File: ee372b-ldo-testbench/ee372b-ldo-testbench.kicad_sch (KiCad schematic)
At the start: 136 parts, among them J1 PEC02SAAN, J10 OUT_S, J11 VOUT, J12 VDD_BUF, J13 V_SIG, J14 PEC03SAAN, J15 VSIG_BUF, J16 PEC03SAAN, J17 PEC03SAAN, J18 PEC03SAAN, J19 PEC03SAAN, J2 PEC02SAAN, J20 VREF_EXTERNAL, J21 PEC02SAAN, J22 PEC02SAAN, J23 PEC02SAAN, J24 PEC02SAAN, J25 PEC03SAAN, J3 GND, J4 1V8, J5 3v3_EXTERNAL, J8 VIN, J9 IN_S, Q1 FDV305N, Q2 FDV305N, Q3 FDV305N, Q4 FDV305N, Q5 FDV305N, U1 MMSZ4679T1G, U3 ADS1220IPW, U4 BUF634AIDR

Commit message: reduced pin bypass caps
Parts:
- removed C24, C9: 100nF, Capacitor_SMD:C_0805_2012Metric_Pad1.18x1.45mm_HandSolder, symbol Device:C_Small_US
- removed R21, R22, R23, R24, R25, R26, R27, R28, R29, R30, R31, R32, R33, R34, R35, R36: 0, Resistor_SMD:R_0805_2012Metric_Pad1.20x1.40mm_HandSolder, symbol Device:R
- added R45, R46: 0, Resistor_SMD:R_0805_2012Metric_Pad1.20x1.40mm_HandSolder, symbol Device:R
- C27: value 1uF -> 100nF
- C6: value 100nF -> 1uF
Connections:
- net GND: now also U2.1 (VSS), U2.13 (VSS), U2.18 (VSS), U2.20 (VSS), U2.22 (VSS), U2.23 (VSS), U2.25 (VSS), U2.26 (VSS), U2.28 (VSS), U2.29 (VSS), U2.3 (VSS), U2.30 (VSS), U2.31 (VSS), U2.4 (VSS), U2.6 (VSS), U2.7 (VSS), R46.2; no longer U3.6 (AIN3/REFN1)
- net c1_vin_jump: now also R45.1; no longer C4.2, U2.2 (VDD)
- net at C23.2, U2.27 (VDD): now also C10.2, C17.2, C27.2, C4.2, C5.2, C6.2, C7.2, U2.14 (VDD), U2.16 (VDD), U2.17 (VDD), U2.2 (VDD), U2.21 (VDD), U2.24 (VDD), U2.32 (VDD), U2.8 (VDD), R45.2
- new net LDO_GND: R46.1, U3.6 (AIN3/REFN1)
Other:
- moved on the sheet: C10, C23, C27, C4, C5, C7

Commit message: added 100mm x 100mm thing
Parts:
- removed J8: VIN, 1_EE372_DemoBoard:CALTEST_CT3151-2, symbol Connector:Conn_01x01_Pin
- removed R57: 0, Resistor_SMD:R_0805_2012Metric_Pad1.20x1.40mm_HandSolder, symbol Device:R
- TP10: value 1V8 -> 3V3
- TP3: value OUT_S1 -> LOAD_OUT
- TP4: value OUT_S2 -> LDO_VOUT
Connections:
- net BGR_VREF: now also R37.2, U2.19 (OTA_VREF)
- net VIN renamed 1V8
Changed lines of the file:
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@@
 	(wire
 		(pts
-			(xy 334.01 115.57) (xy 336.55 115.57)
-		)
-		(stroke
-			(width 0)
-			(type default)
-		)
-	)
-	(wire
-		(pts
 			(xy 377.19 135.89) (xy 379.73 135.89)
 		)
@@
 	(wire
 		(pts
-			(xy 323.85 115.57) (xy 326.39 115.57)
+			(xy 323.85 115.57) (xy 336.55 115.57)
 		)
 		(stroke
@@
 		)
 	)
+	(label "1V8"
+		(at 172.72 80.01 0)
+		(effects
+			(font
+				(size 1.27 1.27)
+			)
+			(justify left bottom)
+		)
+	)
 	(label "pico_spi_tx"
 		(at 365.76 285.75 180)
@@
 			)
 		)
-		(property "Value" "OUT_S1"
+		(property "Value" "LOAD_OUT"
 			(at 523.24 105.9179 0)
 			(show_name no)
@@
 	)
 	(symbol
-		(lib_id "Device:R")
-		(at 330.2 115.57 270)
-		(unit 1)
-		(body_style 1)
-		(exclude_from_sim no)
-		(in_bom yes)
-		(on_board yes)
-		(in_pos_files yes)
-		(dnp no)
-		(fields_autoplaced yes)
-		(property "Reference" "R57"
-			(at 330.2 109.22 90)
-			(show_name no)
-			(do_not_autoplace no)
-			(effects
-				(font
-					(size 1.27 1.27)
-				)
-			)
-		)
-		(property "Value" "0"
-			(at 330.2 111.76 90)
-			(show_name no)
-			(do_not_autoplace no)
-			(effects
-				(font
-					(size 1.27 1.27)
-				)
-			)
-		)
-		(property "Footprint" "Resistor_SMD:R_0805_2012Metric_Pad1.20x1.40mm_HandSolder"
-			(at 330.2 113.792 90)
-			(hide yes)
-			(show_name no)
-			(do_not_autoplace no)
-			(effects
-				(font
-					(size 1.27 1.27)
-				)
-			)
-		)
-		(property "Datasheet" ""
-			(at 330.2 115.57 0)
-			(hide yes)
-			(show_name no)
-			(do_not_autoplace no)
-			(effects
-				(font
-					(size 1.27 1.27)
-				)
-			)
-		)
-		(property "Description" "Resistor"
-			(at 330.2 115.57 0)
-			(hide yes)
-			(show_name no)
-			(do_not_autoplace no)
-			(effects
-				(font
-					(size 1.27 1.27)
-				)
-			)
-		)
-		(pin "1"
-		)
-		(pin "2"
-		)
-		(instances
-			(project "ee372b-ldo-testbench"
-				(path "/4eaac8a8-2761-424f-b17c-d4cc8c253812"
-					(reference "R57")
-					(unit 1)
-				)
-			)
-		)
-	)
-	(symbol
 		(lib_id "power:GND")
 		(at 194.31 92.71 0)
@@
 			)
 		)
-		(property "Value" "OUT_S2"
+		(property "Value" "LDO_VOUT"
 			(at 492.76 104.6479 0)
 			(show_name no)
@@
 	)
 	(symbol
-		(lib_id "Connector:Conn_01x01_Pin")
-		(at 167.64 80.01 0)
-		(unit 1)
-		(body_style 1)
-		(exclude_from_sim no)
-		(in_bom yes)
-		(on_board yes)
-		(in_pos_files yes)
-		(dnp no)
-		(property "Reference" "J8"
-			(at 168.275 74.93 0)
-			(show_name no)
-			(do_not_autoplace no)
-			(effects
-				(font
-					(size 1.27 1.27)
-				)
-			)
-		)
-		(property "Value" "VIN"
-			(at 168.275 77.47 0)
-			(show_name no)
-			(do_not_autoplace no)
-			(effects
-				(font
-					(size 1.27 1.27)
-				)
-			)
-		)
-		(property "Footprint" "1_EE372_DemoBoard:CALTEST_CT3151-2"
-			(at 167.64 80.01 0)
-			(hide yes)
-			(show_name no)
-			(do_not_autoplace no)
-			(effects
-				(font
-					(size 1.27 1.27)
-				)
-			)
-		)
-		(property "Datasheet" "https://mm.digikey.com/Volume0/opasdata/d220001/medias/docus/4846/DS_1768_Catalog.pdf"
-			(at 167.64 80.01 0)
-			(hide yes)
-			(show_name no)
-			(do_not_autoplace no)
-			(effects
-				(font
-					(size 1.27 1.27)
-				)
-			)
-		)
-		(property "Description" "CONN BANANA JACK SOLDER RED"
-			(at 167.64 80.01 0)
-			(hide yes)
-			(show_name no)
-			(do_not_autoplace no)
-			(effects
-				(font
-					(size 1.27 1.27)
-				)
-			)
-		)
-		(property "Manufacturer" "Cal Test Electronics"
-			(at 167.64 80.01 0)
-			(hide yes)
-			(show_name no)
-			(do_not_autoplace no)
-			(effects
-				(font
-					(size 1.27 1.27)
-				)
-			)
-		)
-		(property "Manufacturer Part Number" "CT3151SP-2"
-			(at 167.64 80.01 0)
-			(hide yes)
-			(show_name no)
-			(do_not_autoplace no)
-			(effects
-				(font
-					(size 1.27 1.27)
-				)
-			)
-		)
-		(property "Distributer Link 1" "https://www.digikey.com/en/products/detail/cal-test-electronics/CT3151SP-2/6005547"
-			(at 167.64 80.01 0)
-			(hide yes)
-			(show_name no)
-			(do_not_autoplace no)
-			(effects
-				(font
-					(size 1.27 1.27)
-				)
-			)
-		)
-		(property "Distributer Link 2" "https://www.mouser.com/en/ProductDetail/Cal-Test/CT3151SP-2?qs=vgjKjNJexTiE58m2a2m1iA%3D%3D"
-			(at 167.64 80.01 0)
-			(hide yes)
-			(show_name no)
-			(do_not_autoplace no)
-			(effects
-				(font
-					(size 1.27 1.27)
-				)
-			)
-		)
-		(pin "1"
-		)
-		(instances
-			(project "ee372b-ldo-testbench"
-				(path "/4eaac8a8-2761-424f-b17c-d4cc8c253812"
-					(reference "J8")
-					(unit 1)
-				)
-			)
-		)
-	)
-	(symbol
 		(lib_id "power:GND")
 		(at 434.34 316.23 0)
@@
 			)
 		)
-		(property "Value" "1V8"
+		(property "Value" "3V3"
 			(at 265.43 198.6279 0)
 			(show_name no)

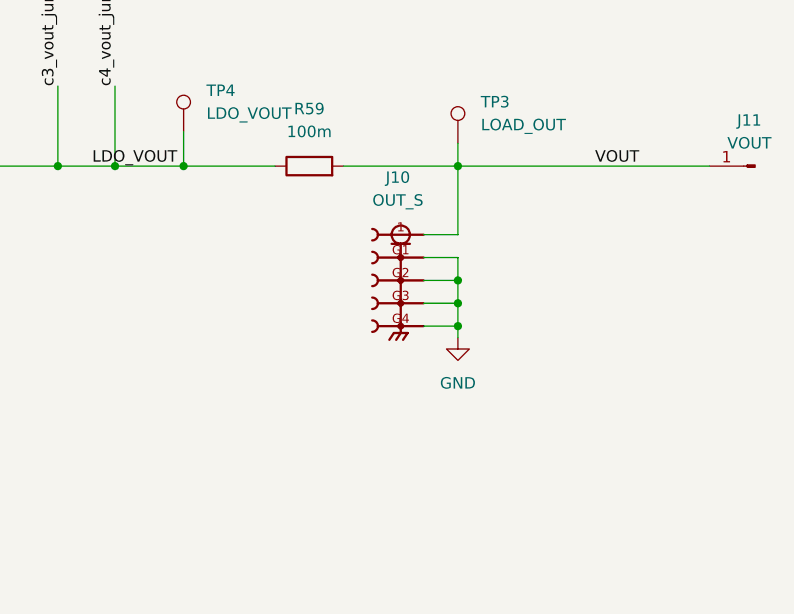
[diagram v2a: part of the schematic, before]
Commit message: added selectable output for ADC Analog3 pin measurement for VOUT
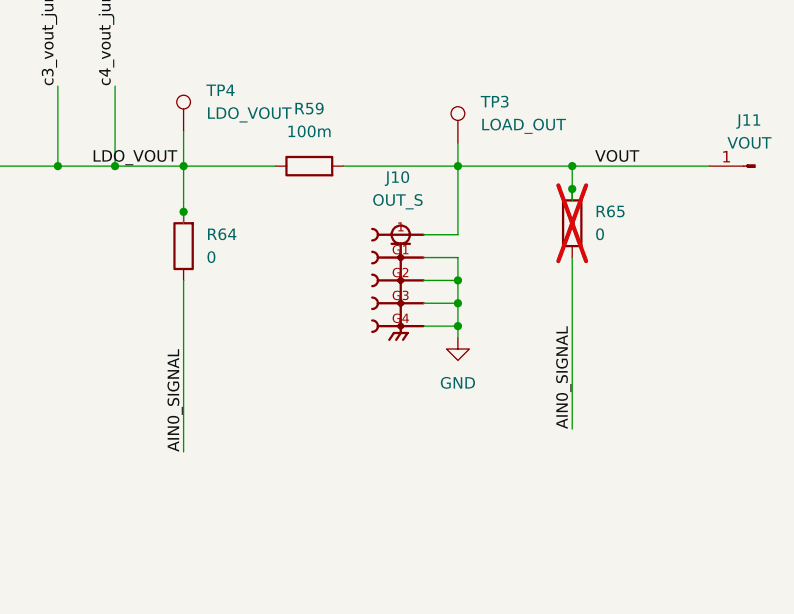
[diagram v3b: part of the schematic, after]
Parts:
- added R64, R65: 0, Resistor_SMD:R_0805_2012Metric_Pad1.20x1.40mm_HandSolder, symbol Device:R
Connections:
- net AIN0_SIGNAL: now also R64.1, R65.1
- net LDO_VOUT: now also R64.2
- net VOUT: now also R65.2

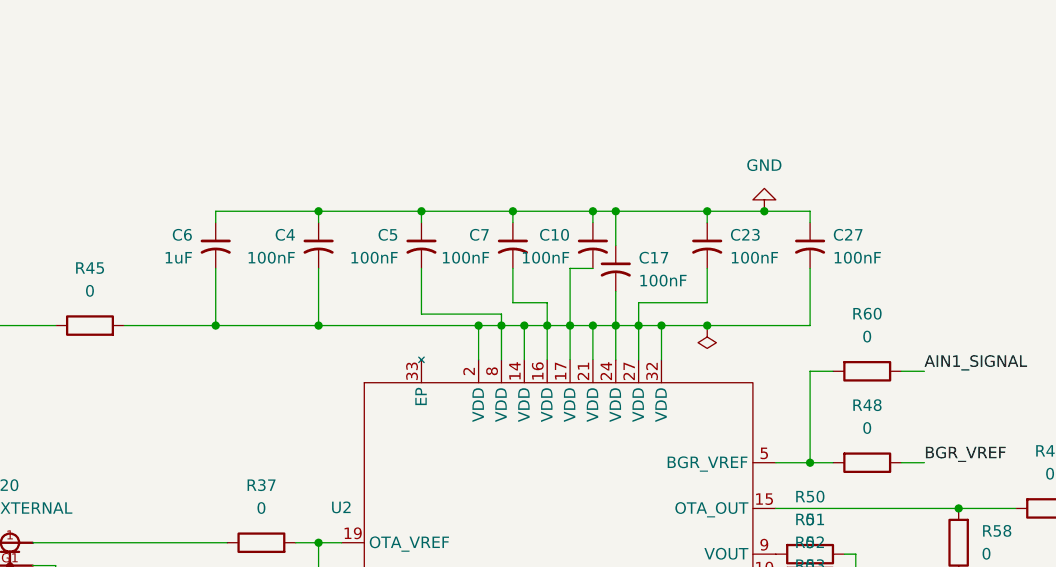
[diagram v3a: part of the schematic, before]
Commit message: re add caps for each pin
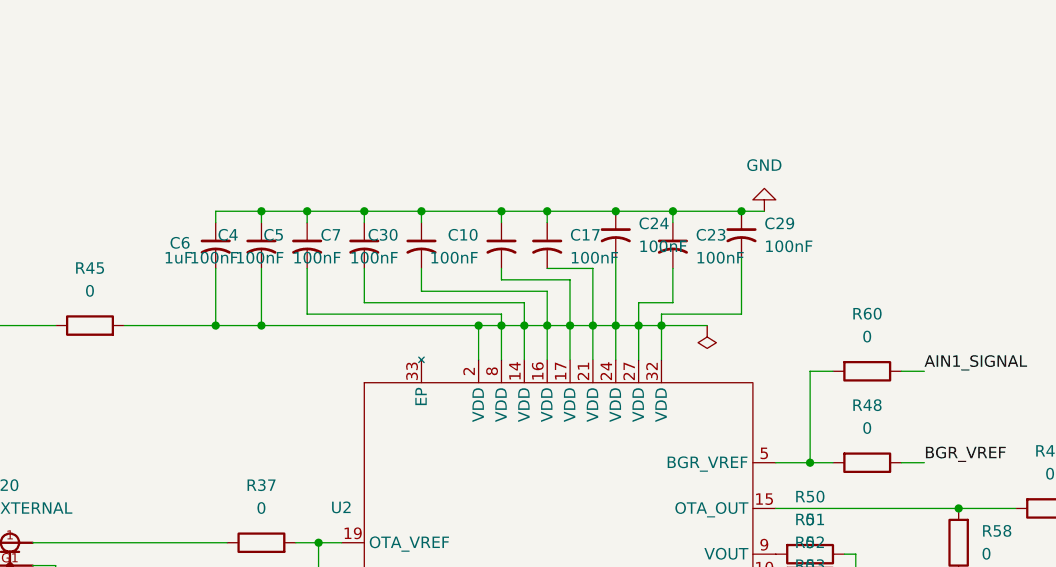
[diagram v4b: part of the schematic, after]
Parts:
- removed C27: 100nF, Capacitor_SMD:C_0805_2012Metric_Pad1.18x1.45mm_HandSolder, symbol Device:C_Small_US
- added C24, C29, C30: 100nF, Capacitor_SMD:C_0805_2012Metric_Pad1.18x1.45mm_HandSolder, symbol Device:C_Small_US
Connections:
- net GND: now also C24.1, C29.1, C30.1
- net at C10.2, C17.2, C23.2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: now also C24.2, C29.2, C30.2
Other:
- moved on the sheet: C10, C17, C23, C4, C5, C7

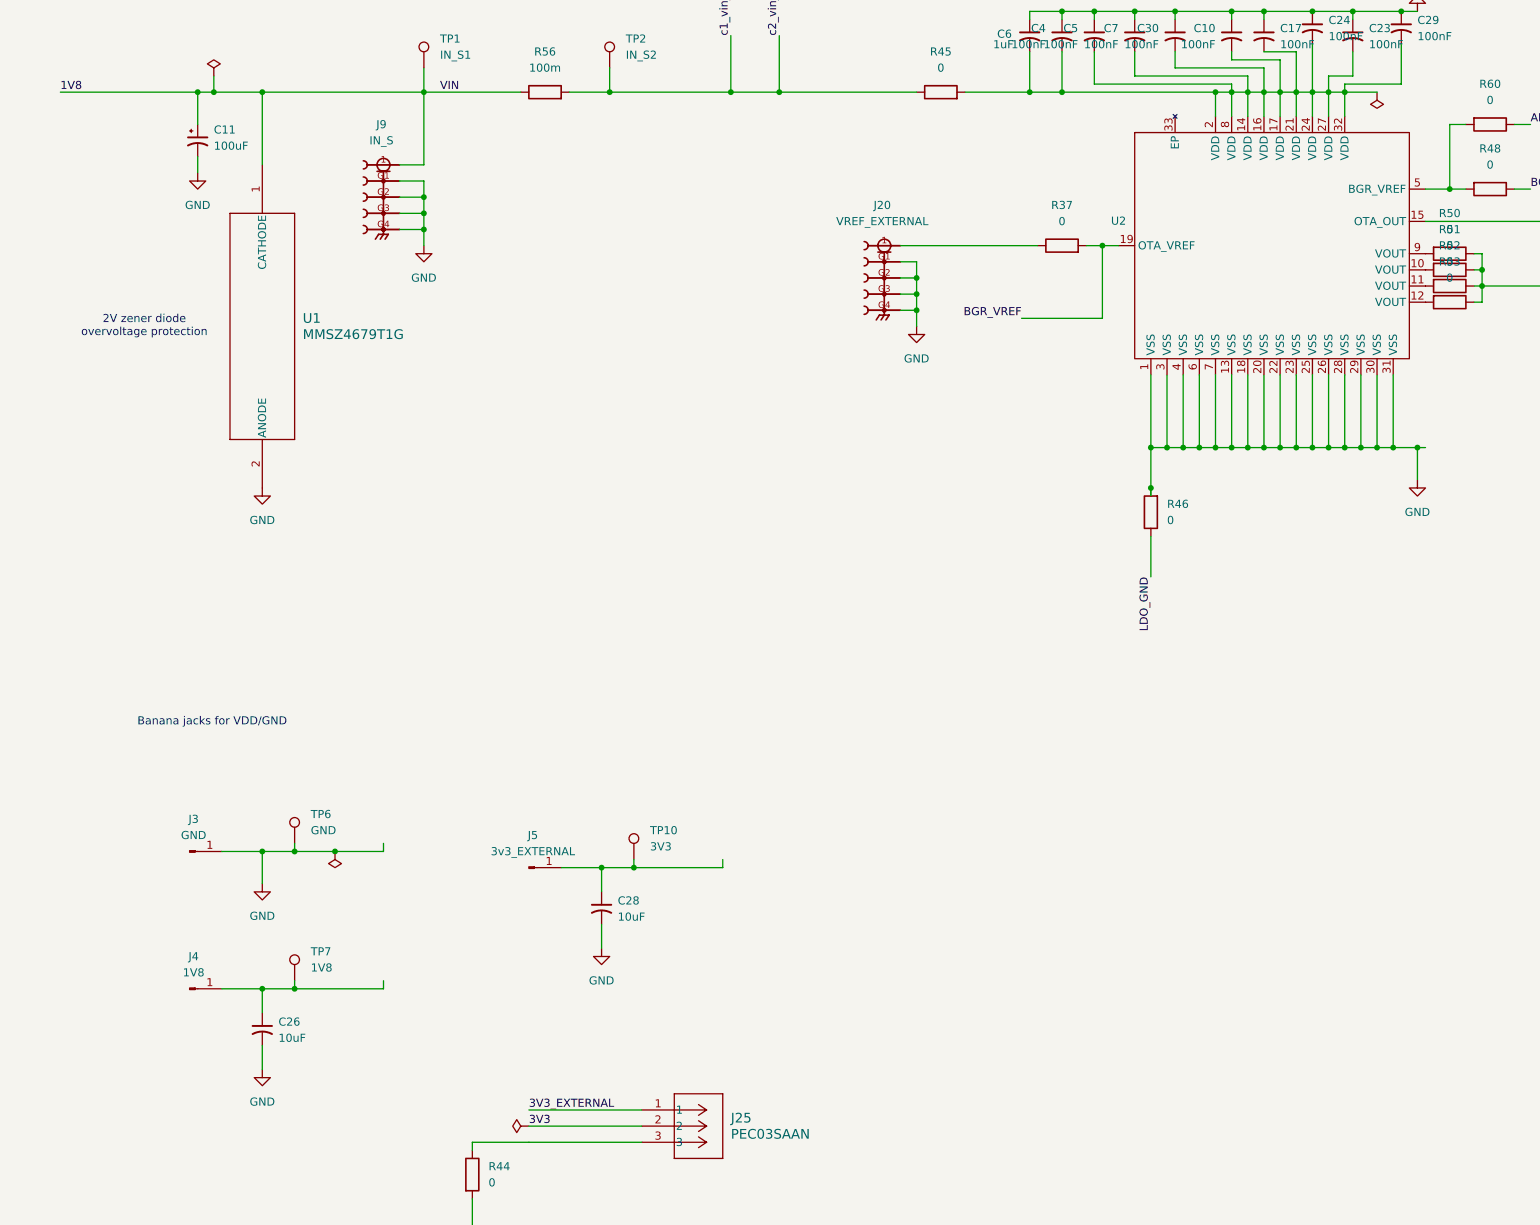
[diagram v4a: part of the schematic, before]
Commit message: added more GND test points and EP to VSS r0 thing
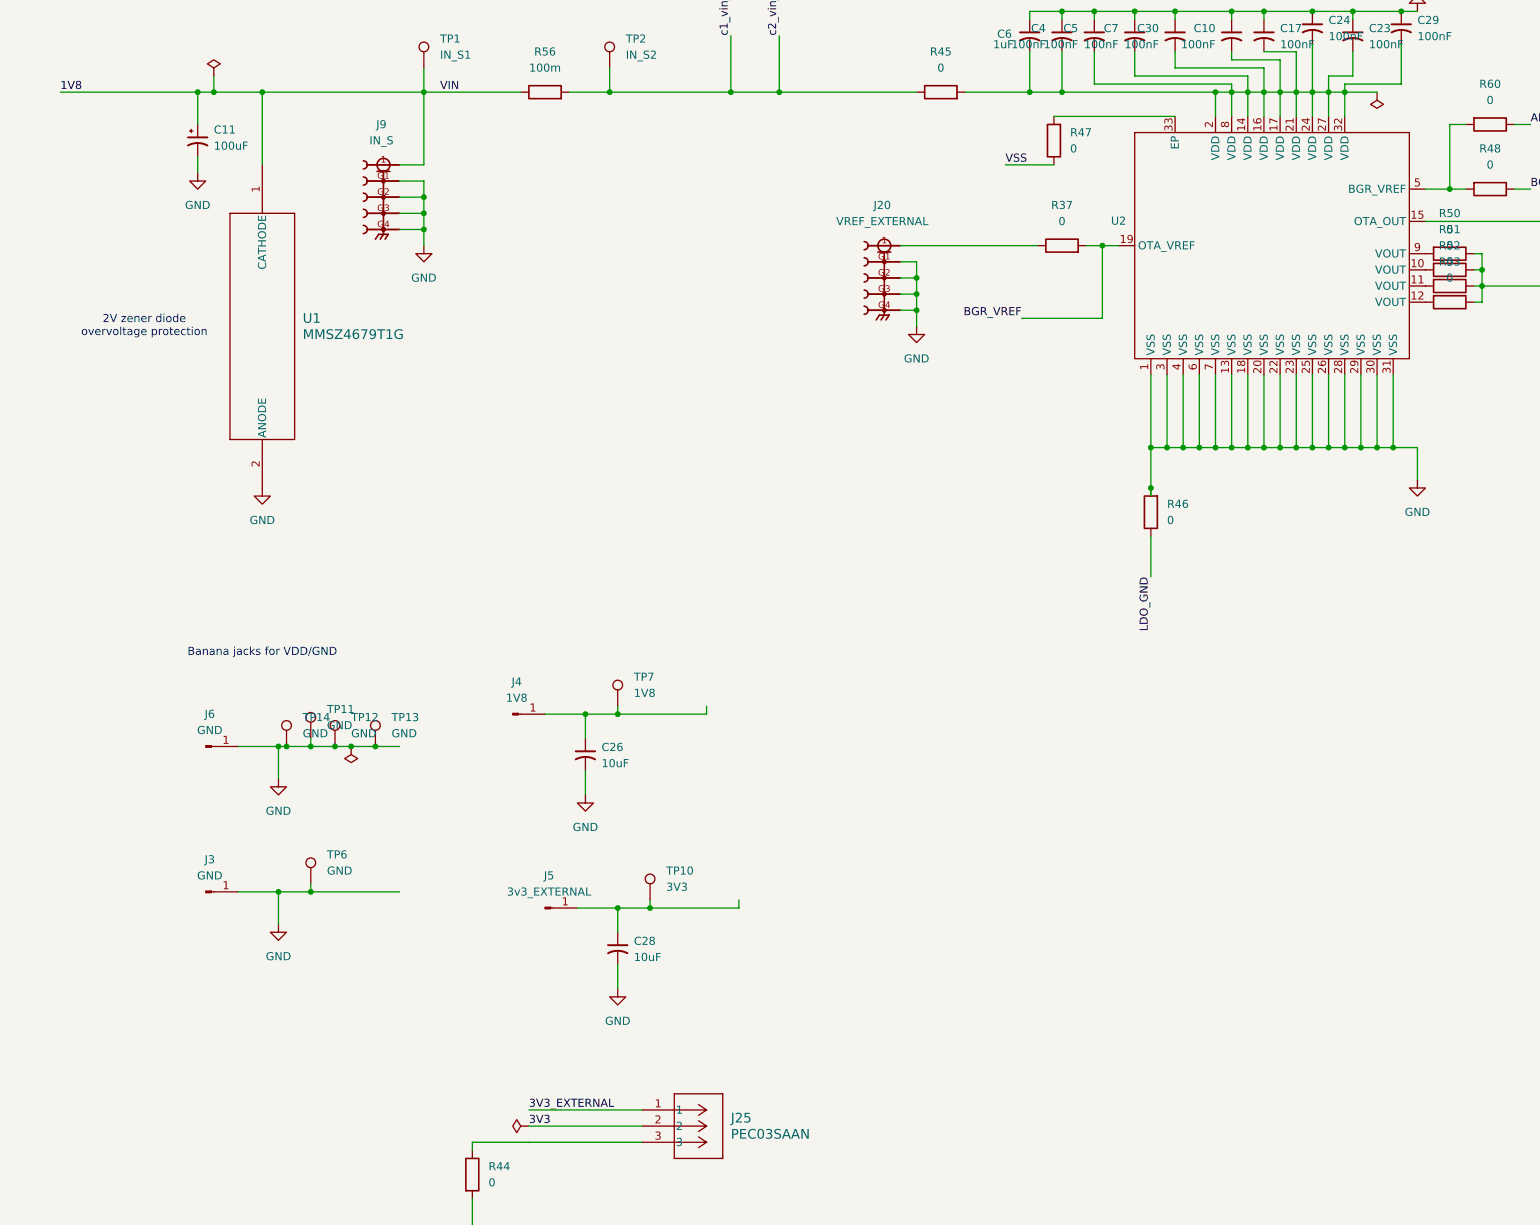
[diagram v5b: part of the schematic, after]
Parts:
- added J6: GND, 1_EE372_DemoBoard:CALTEST_CT3151-2, symbol Connector:Conn_01x01_Pin
- added R47: 0, Resistor_SMD:R_0805_2012Metric_Pad1.20x1.40mm_HandSolder, symbol Device:R
- added TP11, TP12, TP13, TP14: GND, 1_EE372_DemoBoard:KEYSTONE_5016, symbol Connector:TestPoint
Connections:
- net GND: now also J6.1 (Pin_1), TP11.1, TP12.1, TP13.1, TP14.1
- net at U2.33 (EP): now also R47.2
- new net VSS: R47.1
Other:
- moved on the sheet: C26, C28, J3, J4, J5, TP10, TP6, TP7
